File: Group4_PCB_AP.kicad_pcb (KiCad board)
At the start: 2 copper layers, 70 x 70 mm, 58 parts, among them J1 Conn_02x03_Odd_Even, J10 Conn_Coaxial, J11 Conn_Coaxial, J12 Conn_Coaxial, J13 Conn_02x02_Odd_Even, J14 Conn_02x02_Odd_Even, J15 Conn_02x02_Odd_Even, J16 Conn_02x02_Odd_Even, J17 Conn_02x02_Odd_Even, J2 Conn_02x03_Odd_Even, J3 Conn_Coaxial, J4 Conn_Coaxial, J5 Conn_02x03_Odd_Even, J6 Conn_02x03_Odd_Even, J7 Conn_02x02_Odd_Even, J8 Conn_02x02_Odd_Even, J9 Conn_02x03_Odd_Even

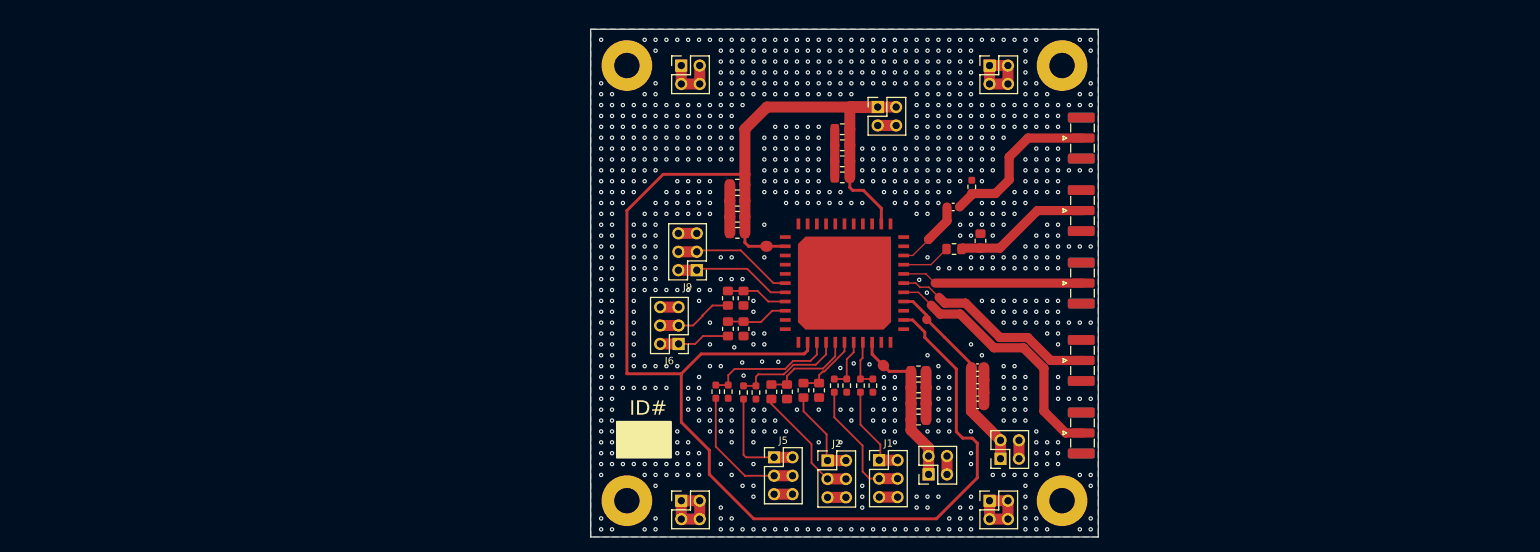
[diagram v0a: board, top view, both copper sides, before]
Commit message: Creating PCB copy in layout
Created PCB layout and tied all the components to the respective components in schematic view.
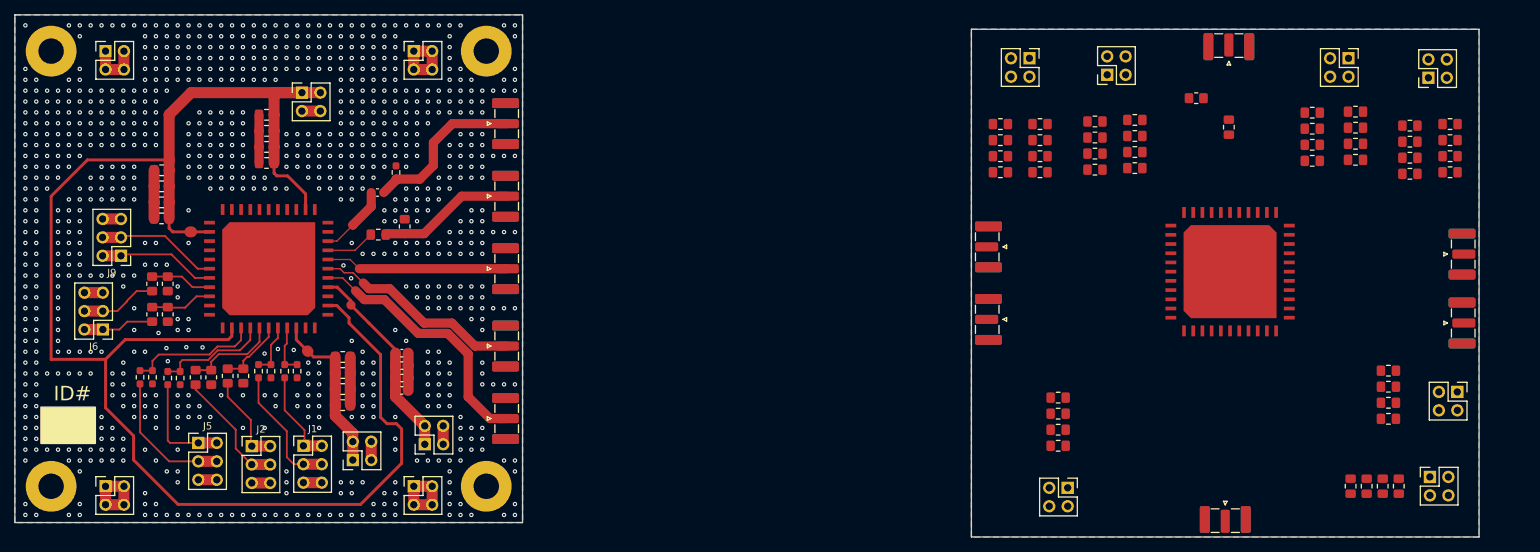
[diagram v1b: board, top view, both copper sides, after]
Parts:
- added C19: 1n, Capacitor_SMD:C_0805_2012Metric_Pad1.18x1.45mm_HandSolder, F.Cu at (208.0, 76.0)
- added C20: 22p, Capacitor_SMD:C_0805_2012Metric_Pad1.18x1.45mm_HandSolder, F.Cu at (231.4, 125.5)
- added C21: 2.2n, Capacitor_SMD:C_0805_2012Metric_Pad1.18x1.45mm_HandSolder, F.Cu at (229.2, 125.5)
- added C22: 0.22u, Capacitor_SMD:C_0805_2012Metric_Pad1.18x1.45mm_HandSolder, F.Cu at (227.0, 125.5)
- added C23: 22u, Capacitor_SMD:C_0805_2012Metric_Pad1.18x1.45mm_HandSolder, F.Cu at (224.8, 125.5)
- added C24: 22p, Capacitor_SMD:C_0805_2012Metric_Pad1.18x1.45mm_HandSolder, F.Cu at (230.0, 116.2)
- added C25: 2.2n, Capacitor_SMD:C_0805_2012Metric_Pad1.18x1.45mm_HandSolder, F.Cu at (230.0, 114.0)
- added C26: 0.22u, Capacitor_SMD:C_0805_2012Metric_Pad1.18x1.45mm_HandSolder, F.Cu at (230.0, 111.8)
- added C27: 22u, Capacitor_SMD:C_0805_2012Metric_Pad1.18x1.45mm_HandSolder, F.Cu at (230.0, 109.6)
- added C28: 22p, Capacitor_SMD:C_0805_2012Metric_Pad1.18x1.45mm_HandSolder, F.Cu at (176.5, 82.2)
- added C29: 22p, Capacitor_SMD:C_0805_2012Metric_Pad1.18x1.45mm_HandSolder, F.Cu at (182.0, 75.6)
- added C30: 2.2n, Capacitor_SMD:C_0805_2012Metric_Pad1.18x1.45mm_HandSolder, F.Cu at (176.5, 80.0)
- added C31: 2.2n, Capacitor_SMD:C_0805_2012Metric_Pad1.18x1.45mm_HandSolder, F.Cu at (182.0, 77.8)
- added C32: 0.22u, Capacitor_SMD:C_0805_2012Metric_Pad1.18x1.45mm_HandSolder, F.Cu at (176.5, 77.8)
- added C33: 0.22u, Capacitor_SMD:C_0805_2012Metric_Pad1.18x1.45mm_HandSolder, F.Cu at (182.0, 80.0)
- added C34: 22u, Capacitor_SMD:C_0805_2012Metric_Pad1.18x1.45mm_HandSolder, F.Cu at (176.5, 75.6)
- added C35: 22u, Capacitor_SMD:C_0805_2012Metric_Pad1.18x1.45mm_HandSolder, F.Cu at (182.0, 82.2)
- added C36: 22p, Capacitor_SMD:C_0805_2012Metric_Pad1.18x1.45mm_HandSolder, F.Cu at (189.5, 81.9)
- added C37: 22p, Capacitor_SMD:C_0805_2012Metric_Pad1.18x1.45mm_HandSolder, F.Cu at (195.0, 75.0)
- added C38: 2.2n, Capacitor_SMD:C_0805_2012Metric_Pad1.18x1.45mm_HandSolder, F.Cu at (189.5, 79.6)
- added C39: 2.2n, Capacitor_SMD:C_0805_2012Metric_Pad1.18x1.45mm_HandSolder, F.Cu at (195.0, 77.2)
- added C40: 0.22u, Capacitor_SMD:C_0805_2012Metric_Pad1.18x1.45mm_HandSolder, F.Cu at (189.5, 77.4)
- added C41: 0.22u, Capacitor_SMD:C_0805_2012Metric_Pad1.18x1.45mm_HandSolder, F.Cu at (195.0, 79.4)
- added C42: 22u, Capacitor_SMD:C_0805_2012Metric_Pad1.18x1.45mm_HandSolder, F.Cu at (189.5, 75.2)
- added C43: 22u, Capacitor_SMD:C_0805_2012Metric_Pad1.18x1.45mm_HandSolder, F.Cu at (195.0, 81.6)
- added C44: 22p, Capacitor_SMD:C_0805_2012Metric_Pad1.18x1.45mm_HandSolder, F.Cu at (233.0, 82.4)
- added C45: 22p, Capacitor_SMD:C_0805_2012Metric_Pad1.18x1.45mm_HandSolder, F.Cu at (238.5, 75.6)
- added C46: 2.2n, Capacitor_SMD:C_0805_2012Metric_Pad1.18x1.45mm_HandSolder, F.Cu at (233.0, 80.2)
- added C47: 2.2n, Capacitor_SMD:C_0805_2012Metric_Pad1.18x1.45mm_HandSolder, F.Cu at (238.5, 77.8)
- added C48: 0.22u, Capacitor_SMD:C_0805_2012Metric_Pad1.18x1.45mm_HandSolder, F.Cu at (233.0, 78.0)
- added C49: 0.22u, Capacitor_SMD:C_0805_2012Metric_Pad1.18x1.45mm_HandSolder, F.Cu at (238.5, 80.0)
- added C50: 22u, Capacitor_SMD:C_0805_2012Metric_Pad1.18x1.45mm_HandSolder, F.Cu at (233.0, 75.8)
- added C51: 22u, Capacitor_SMD:C_0805_2012Metric_Pad1.18x1.45mm_HandSolder, F.Cu at (238.5, 82.2)
- added C52: 22p, Capacitor_SMD:C_0805_2012Metric_Pad1.18x1.45mm_HandSolder, F.Cu at (219.5, 80.6)
- added C53: 22p, Capacitor_SMD:C_0805_2012Metric_Pad1.18x1.45mm_HandSolder, F.Cu at (225.5, 73.9)
- added C54: 2.2n, Capacitor_SMD:C_0805_2012Metric_Pad1.18x1.45mm_HandSolder, F.Cu at (219.5, 78.4)
- added C55: 2.2n, Capacitor_SMD:C_0805_2012Metric_Pad1.18x1.45mm_HandSolder, F.Cu at (225.5, 76.1)
- added C56: 0.22u, Capacitor_SMD:C_0805_2012Metric_Pad1.18x1.45mm_HandSolder, F.Cu at (219.5, 76.2)
- added C57: 0.22u, Capacitor_SMD:C_0805_2012Metric_Pad1.18x1.45mm_HandSolder, F.Cu at (225.5, 78.3)
- added C58: 22u, Capacitor_SMD:C_0805_2012Metric_Pad1.18x1.45mm_HandSolder, F.Cu at (219.5, 74.0)
- added C59: 22u, Capacitor_SMD:C_0805_2012Metric_Pad1.18x1.45mm_HandSolder, F.Cu at (225.5, 80.5)
- added C60: 22p, Capacitor_SMD:C_0805_2012Metric_Pad1.18x1.45mm_HandSolder, F.Cu at (184.5, 119.9)
- added C61: 2.2n, Capacitor_SMD:C_0805_2012Metric_Pad1.18x1.45mm_HandSolder, F.Cu at (184.5, 117.7)
- added C62: 0.22u, Capacitor_SMD:C_0805_2012Metric_Pad1.18x1.45mm_HandSolder, F.Cu at (184.5, 115.5)
- added C63: 22u, Capacitor_SMD:C_0805_2012Metric_Pad1.18x1.45mm_HandSolder, F.Cu at (184.5, 113.3)
- added J18: Conn_Coaxial, Connector_Coaxial:SMA_Samtec_SMA-J-P-H-ST-EM1_EdgeMount, F.Cu at (208.0, 64.7)
- added J19: Conn_Coaxial, Connector_Coaxial:SMA_Samtec_SMA-J-P-H-ST-EM1_EdgeMount, F.Cu at (207.5, 130.3)
- added J20: Conn_02x02_Odd_Even, Connector_PinHeader_2.54mm:PinHeader_2x02_P2.54mm_Vertical, F.Cu at (235.7, 124.2)
- added J21: Conn_02x02_Odd_Even, Connector_PinHeader_2.54mm:PinHeader_2x02_P2.54mm_Vertical, F.Cu at (239.5, 112.5)
- added J22: Conn_Coaxial, Connector_Coaxial:SMA_Samtec_SMA-J-P-H-ST-EM1_EdgeMount, F.Cu at (240.4, 103.0)
- added J23: Conn_Coaxial, Connector_Coaxial:SMA_Samtec_SMA-J-P-H-ST-EM1_EdgeMount, F.Cu at (240.4, 93.5)
- added J24: Conn_02x02_Odd_Even, Connector_PinHeader_2.54mm:PinHeader_2x02_P2.54mm_Vertical, F.Cu at (180.5, 66.5)
- added J25: Conn_02x02_Odd_Even, Connector_PinHeader_2.54mm:PinHeader_2x02_P2.54mm_Vertical, F.Cu at (191.2, 68.8)
- added J26: Conn_02x02_Odd_Even, Connector_PinHeader_2.54mm:PinHeader_2x02_P2.54mm_Vertical, F.Cu at (235.5, 69.2)
- added J27: Conn_02x02_Odd_Even, Connector_PinHeader_2.54mm:PinHeader_2x02_P2.54mm_Vertical, F.Cu at (224.5, 66.5)
- added J28: Conn_02x02_Odd_Even, Connector_PinHeader_2.54mm:PinHeader_2x02_P2.54mm_Vertical, F.Cu at (185.8, 125.7)
- added J29: Conn_Coaxial, Connector_Coaxial:SMA_Samtec_SMA-J-P-H-ST-EM1_EdgeMount, F.Cu at (174.6, 92.5)
- added J30: Conn_Coaxial, Connector_Coaxial:SMA_Samtec_SMA-J-P-H-ST-EM1_EdgeMount, F.Cu at (174.6, 102.5)
- added R19: 51, Resistor_SMD:R_0805_2012Metric_Pad1.20x1.40mm_HandSolder, F.Cu at (203.5, 72.0)
- added U1: ~, CCJ04403:CCJ04403, F.Cu at (208.2, 95.9)
- moved C10 79.4 mm to (85.8, 114.3)
- moved C7 79.4 mm to (85.8, 107.7)
- moved C8 79.4 mm to (85.8, 109.9)
- moved C9 79.4 mm to (85.8, 112.1)
- moved R10 79.4 mm to (94.4, 89.7)
- moved R15 79.4 mm to (61.7, 101.8)
- moved R17 79.4 mm to (61.7, 97.6)
- moved R3 79.4 mm to (74.2, 109.6)
- moved R4 79.4 mm to (75.9, 109.6)
- moved R6 79.4 mm to (72.1, 110.3)
- moved R8 79.4 mm to (67.7, 110.5)
- moved R9 79.4 mm to (93.2, 82.2)
- moved ? 79.4 mm to (45.6, 125.5)
- moved ? 79.4 mm to (108.1, 63.0)
- moved ? 79.4 mm to (105.6, 125.5)
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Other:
- board size 70 x 70 mm -> 201.9 x 72 mm

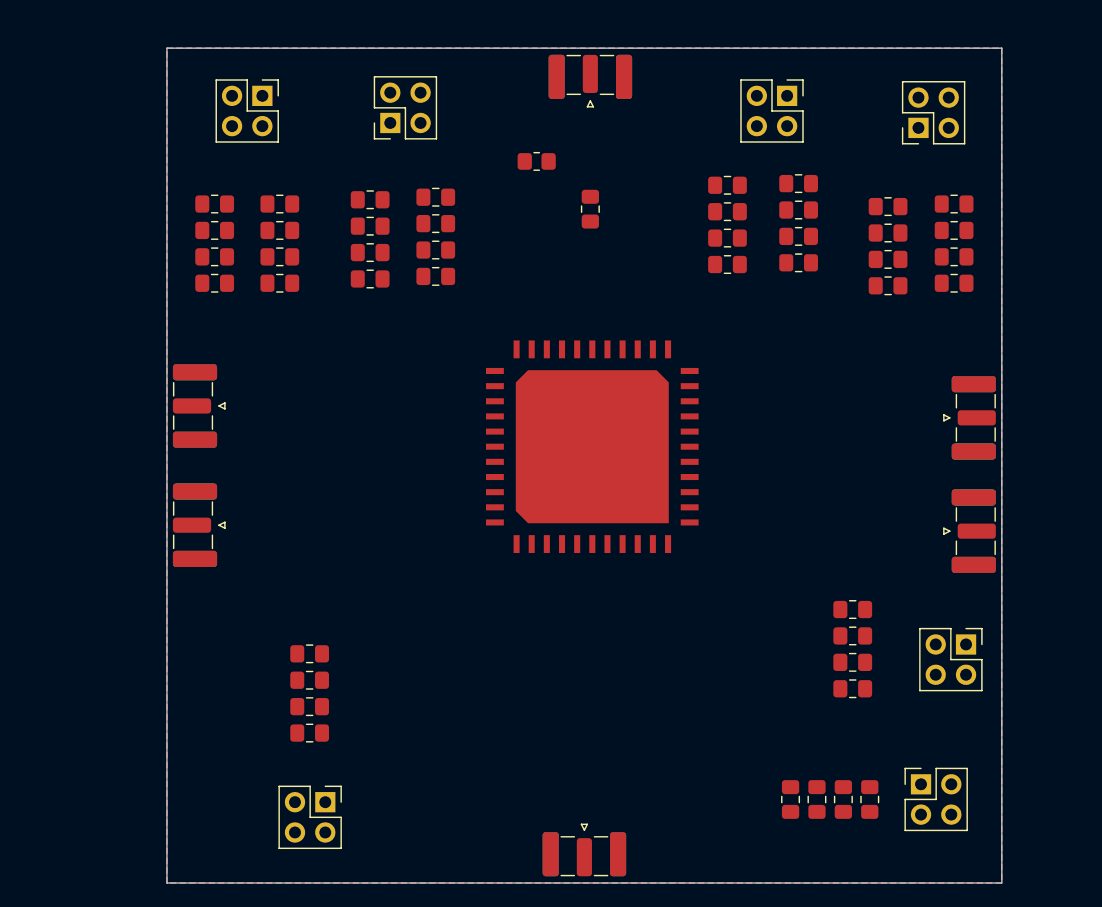
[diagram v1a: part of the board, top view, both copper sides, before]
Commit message: Reorganized layout
Reorganized layout and updated nets and chip symbol to reflect proper pinout
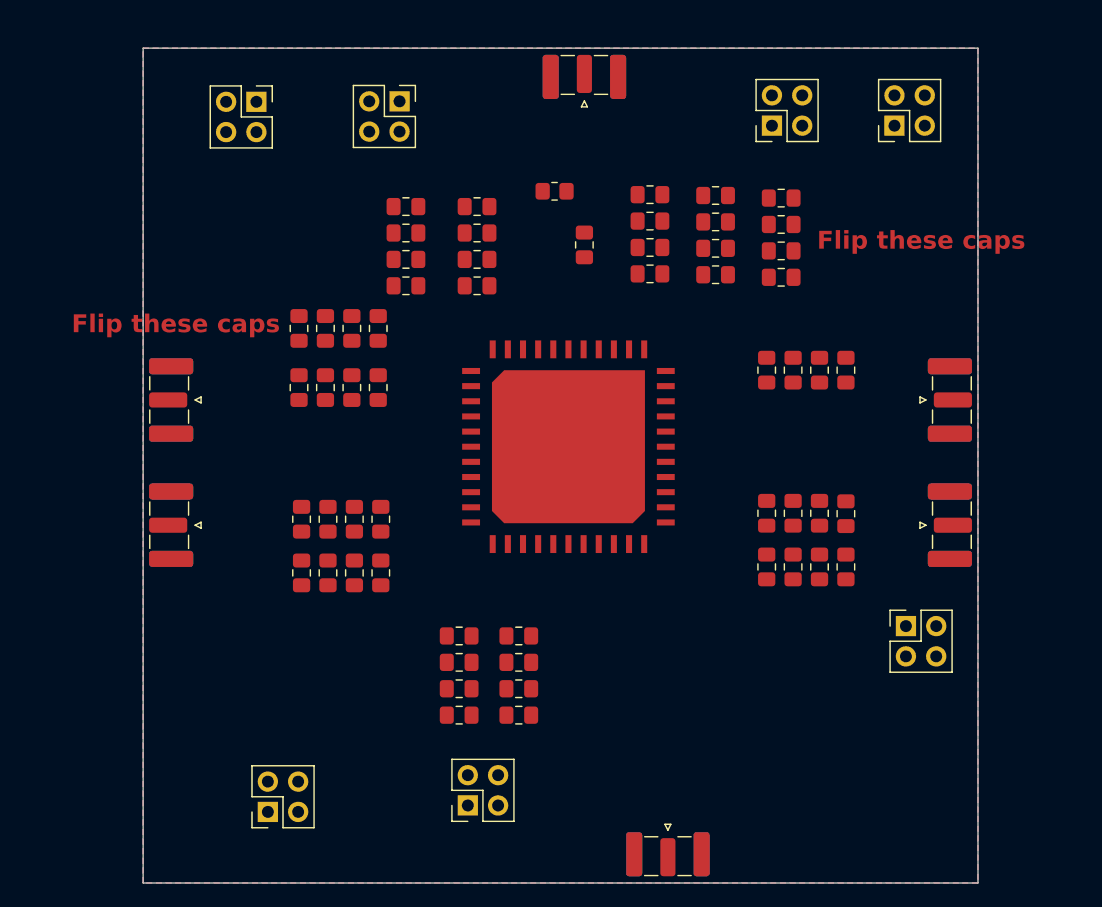
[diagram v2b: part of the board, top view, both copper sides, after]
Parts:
- added C64: 22p, Capacitor_SMD:C_0805_2012Metric_Pad1.18x1.45mm_HandSolder, F.Cu at (222.8, 106.0)
- added C65: 22p, Capacitor_SMD:C_0805_2012Metric_Pad1.18x1.45mm_HandSolder, F.Cu at (183.6, 91.0)
- added C66: 2.2n, Capacitor_SMD:C_0805_2012Metric_Pad1.18x1.45mm_HandSolder, F.Cu at (225.0, 106.0)
- added C67: 2.2n, Capacitor_SMD:C_0805_2012Metric_Pad1.18x1.45mm_HandSolder, F.Cu at (185.8, 91.0)
- added C68: 0.22u, Capacitor_SMD:C_0805_2012Metric_Pad1.18x1.45mm_HandSolder, F.Cu at (227.2, 106.0)
- added C69: 0.22u, Capacitor_SMD:C_0805_2012Metric_Pad1.18x1.45mm_HandSolder, F.Cu at (188.0, 91.0)
- added C70: 22u, Capacitor_SMD:C_0805_2012Metric_Pad1.18x1.45mm_HandSolder, F.Cu at (229.4, 106.0)
- added C71: 22u, Capacitor_SMD:C_0805_2012Metric_Pad1.18x1.45mm_HandSolder, F.Cu at (190.2, 91.0)
- added C72: 22p, Capacitor_SMD:C_0805_2012Metric_Pad1.18x1.45mm_HandSolder, F.Cu at (197.0, 111.8)
- added C73: 2.2n, Capacitor_SMD:C_0805_2012Metric_Pad1.18x1.45mm_HandSolder, F.Cu at (197.0, 114.0)
- added C74: 0.22u, Capacitor_SMD:C_0805_2012Metric_Pad1.18x1.45mm_HandSolder, F.Cu at (197.0, 116.2)
- added C75: 22u, Capacitor_SMD:C_0805_2012Metric_Pad1.18x1.45mm_HandSolder, F.Cu at (197.0, 118.4)
- moved J24 60.0 mm to (181.0, 126.5), turned to 90 degrees
- moved C45 55.9 mm to (183.6, 86.0), turned to 90 degrees
- moved C47 53.4 mm to (185.8, 86.0), turned to 90 degrees
- moved C49 50.9 mm to (188.0, 86.0), turned to 90 degrees
- moved C51 48.4 mm to (190.2, 86.0), turned to 90 degrees
- moved J21 46.4 mm to (223.2, 69.0), turned to 90 degrees
- moved C24 44.8 mm to (213.0, 74.8), turned to 0 degrees
- moved C25 40.7 mm to (213.0, 77.0), turned to 0 degrees
- moved C26 36.7 mm to (213.0, 79.2), turned to 0 degrees
- moved C43 35.3 mm to (229.4, 89.5), turned to 90 degrees
- moved C41 33.7 mm to (227.2, 89.5), turned to 90 degrees
- moved C27 32.9 mm to (213.0, 81.4), turned to 0 degrees
- moved J27 32.5 mm to (192.0, 67.0)
- moved C39 32.4 mm to (225.0, 89.5), turned to 90 degrees
- moved C34 31.8 mm to (183.8, 106.5), turned to -90 degrees
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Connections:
- C19 pad 1: /SMA_SB_0805_IN -> /CK_CHIP
- C19 pad 2: /SMA_SB_0805_INN -> /CK
- C20 pad 1: /VDD_0805 -> /BIAS_LNA
- C21 pad 1: /VDD_0805 -> /BIAS_LNA
- C22 pad 1: /VDD_0805 -> /BIAS_LNA
- C23 pad 1: /VDD_0805 -> /BIAS_LNA
- C24 pad 1: /VDD_0805 -> /BIAS_MIXER
- C25 pad 1: /VDD_0805 -> /BIAS_MIXER
- C26 pad 1: /VDD_0805 -> /BIAS_MIXER
- C27 pad 1: /VDD_0805 -> /BIAS_MIXER
- C28 pad 1: /VDD -> /VDD_LNA
- C29 pad 1: /VDD -> /VDD_LNA
- C30 pad 1: /VDD -> /VDD_LNA
- C31 pad 1: /VDD -> /VDD_LNA
- C32 pad 1: /VDD -> /VDD_LNA
- C33 pad 1: /VDD -> /VDD_LNA
- C34 pad 1: /VDD -> /VDD_LNA
- C35 pad 1: /VDD -> /VDD_LNA
- C36 pad 1: /VDD -> /VDD_MIX
- C37 pad 1: /VDD -> /VDD_MIX
- C38 pad 1: /VDD -> /VDD_MIX
- C39 pad 1: /VDD -> /VDD_MIX
- C40 pad 1: /VDD -> /VDD_MIX
- C41 pad 1: /VDD -> /VDD_MIX
- C42 pad 1: /VDD -> /VDD_MIX
- C43 pad 1: /VDD -> /VDD_MIX
- C44 pad 1: /VDD -> /VDD_DIV
- C45 pad 1: /VDD -> /VDD_DIV
- C46 pad 1: /VDD -> /VDD_DIV
- C47 pad 1: /VDD -> /VDD_DIV
- C48 pad 1: /VDD -> /VDD_DIV
- C49 pad 1: /VDD -> /VDD_DIV
- C50 pad 1: /VDD -> /VDD_DIV
- C51 pad 1: /VDD -> /VDD_DIV
- C52 pad 1: /VDD -> /VDD_BB
- C53 pad 1: /VDD -> /VDD_BB
- C54 pad 1: /VDD -> /VDD_BB
- C55 pad 1: /VDD -> /VDD_BB
- C56 pad 1: /VDD -> /VDD_BB
- C57 pad 1: /VDD -> /VDD_BB
- C58 pad 1: /VDD -> /VDD_BB
- C59 pad 1: /VDD -> /VDD_BB
- C60 pad 1: /VDD_0805 -> /DQ_EN
- C61 pad 1: /VDD_0805 -> /DQ_EN
- C62 pad 1: /VDD_0805 -> /DQ_EN
- C63 pad 1: /VDD_0805 -> /DQ_EN
- J18 pad 1: /SMA_SB_0805_IN -> /CK_CHIP
- J19 pad 1: (no net) -> /SMA_VIN_RF
- J19 pad 2: (no net) -> /GND
- J20 pad 1: /VDD_0805 -> /BIAS_LNA
- J20 pad 2: /VDD_0805 -> /BIAS_LNA
- J21 pad 1: /VDD_0805 -> /BIAS_MIXER
- J21 pad 2: /VDD_0805 -> /BIAS_MIXER
- J22 pad 1: (no net) -> /V_BB_I_P
- J22 pad 2: (no net) -> /GND
- J23 pad 1: (no net) -> /V_BB_I_N
- J23 pad 2: (no net) -> /GND
- J24 pad 1: /VDD -> /VDD_LNA
- J24 pad 2: /VDD -> /VDD_LNA
- J25 pad 1: /VDD -> /VDD_MIX
- J25 pad 2: /VDD -> /VDD_MIX
- J26 pad 1: /VDD -> /VDD_DIV
- J26 pad 2: /VDD -> /VDD_DIV
- J27 pad 1: /VDD -> /VDD_BB
- J27 pad 2: /VDD -> /VDD_BB
- J28 pad 1: /VDD_0805 -> /DQ_EN
- J28 pad 2: /VDD_0805 -> /DQ_EN
- J29 pad 1: (no net) -> /V_BB_Q_P
- J29 pad 2: (no net) -> /GND
- J30 pad 1: (no net) -> /V_BB_Q_N
- J30 pad 2: (no net) -> /GND
- R19 pad 1: /SMA_SB_0805_IN -> /CK_CHIP
- U1 pad 0: (no net) -> /GND
- U1 pad 1: (no net) -> /GND
- U1 pad 10: (no net) -> /VIN_RF
- U1 pad 11: (no net) -> /GND
- U1 pad 12: (no net) -> /GND
- U1 pad 13: (no net) -> /GND
- U1 pad 14: (no net) -> /GND
- U1 pad 15: (no net) -> /DQ_EN
- U1 pad 16: (no net) -> /VDD_DIV
- U1 pad 17: (no net) -> /VDD_LNA
- U1 pad 18: (no net) -> /GND
- U1 pad 19: (no net) -> /VDD_LNA
- U1 pad 2: (no net) -> /VDD_MIX
- U1 pad 20: (no net) -> /V_BB_Q_N
- U1 pad 21: (no net) -> /V_BB_Q_P
- U1 pad 22: (no net) -> /VDD_DIV
- U1 pad 23: (no net) -> /GND
- U1 pad 24: (no net) -> /VDD_DIV
- U1 pad 25: (no net) -> /GND
- U1 pad 26: (no net) -> /VDD_MIX
- U1 pad 27: (no net) -> /VDD_BB
- U1 pad 28: (no net) -> /GND
- U1 pad 29: (no net) -> /CK
- U1 pad 3: (no net) -> /GND
- U1 pad 30: (no net) -> /BIAS_MIXER
- U1 pad 31: (no net) -> /VDD_BB
- U1 pad 32: (no net) -> /VDD_DIV
- U1 pad 4: (no net) -> /V_BB_I_N
- U1 pad 5: (no net) -> /V_BB_I_P
- U1 pad 6: (no net) -> /BIAS_LNA
- U1 pad 7: (no net) -> /GND
- U1 pad 8: (no net) -> /VDD_DIV
- U1 pad 9: (no net) -> /GND
- U1 pad 1: /SMA_SB_0603_INN -> /GND
- U1 pad 10: /A0_1p8V -> /VIN_RF
- U1 pad 11: /A1_1p8V -> /GND
- U1 pad 12: /B0_1p8V -> /GND
- U1 pad 13: /B1_1p8V -> /GND
- U1 pad 14: /C0_1p8V -> /GND
- U1 pad 15: /C1_1p8V -> /DQ_EN
- U1 pad 16: /VDD -> /VDD_DIV
- U1 pad 17: /D0_1p8V -> /VDD_LNA
- U1 pad 18: /D1_1p8V -> /GND
- U1 pad 19: /E0 -> /VDD_LNA
- U1 pad 2: /SMA_SB_0805_INN -> /VDD_MIX
- U1 pad 20: /E1 -> /V_BB_Q_N
- U1 pad 21: /GND -> /V_BB_Q_P
- U1 pad 22: /GND -> /VDD_DIV
- U1 pad 24: /VDD -> /VDD_DIV
- U1 pad 26: /GND -> /VDD_MIX
- U1 pad 27: /GND -> /VDD_BB
- U1 pad 29: /GND -> /CK
- U1 pad 3: /SMA_SE -> /GND
- U1 pad 30: /GND -> /BIAS_MIXER
- U1 pad 31: /GND -> /VDD_BB
- U1 pad 32: /VDD -> /VDD_DIV
- U1 pad 4: /SMA_DIFF_P -> /V_BB_I_N
- U1 pad 5: /SMA_DIFF_N -> /V_BB_I_P
- U1 pad 6: /VDD_0603 -> /BIAS_LNA
- U1 pad 8: /VDD -> /VDD_DIV
- U1 pad 9: /VDD_0805 -> /GND
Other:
- board size 201.9 x 72 mm -> 199.9 x 72 mm
- board text added: "Flip these caps"
